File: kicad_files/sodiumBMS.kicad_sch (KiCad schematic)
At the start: 14 parts, among them J1 USB_C_Receptacle_PowerOnly_6P, U1 STM32F446RETx

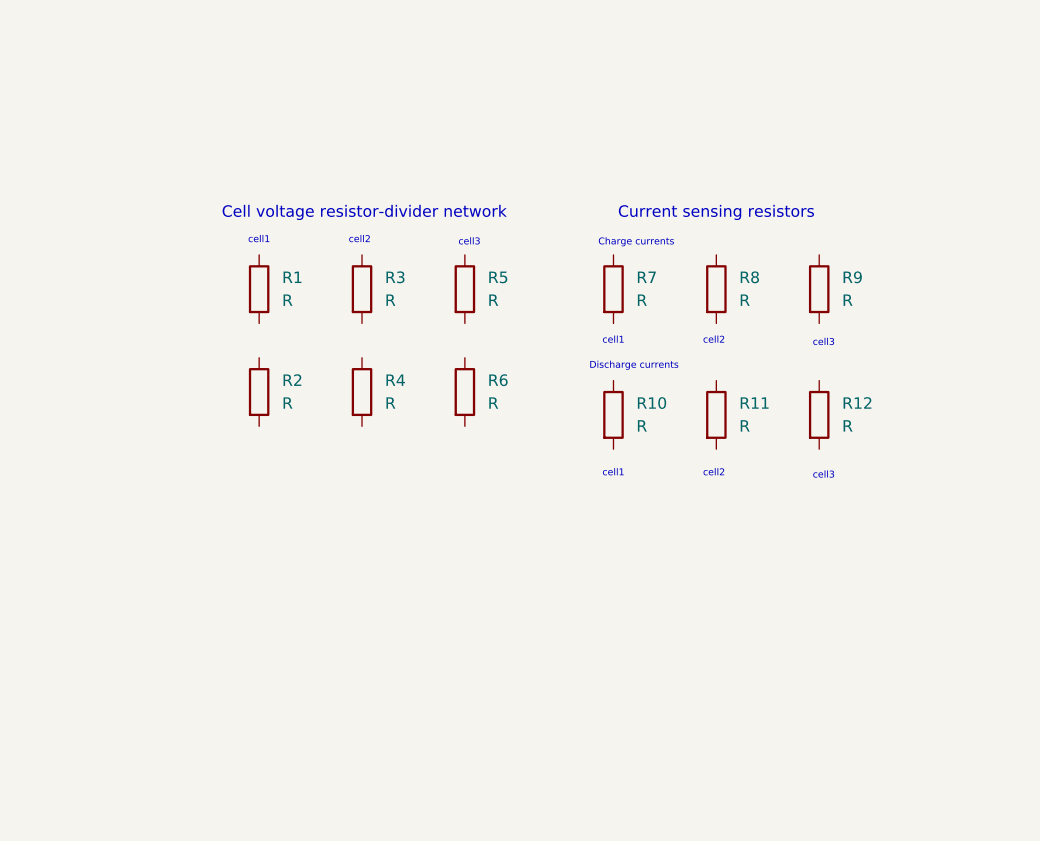
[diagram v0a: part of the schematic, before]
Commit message: added outputs for current and voltage sensing
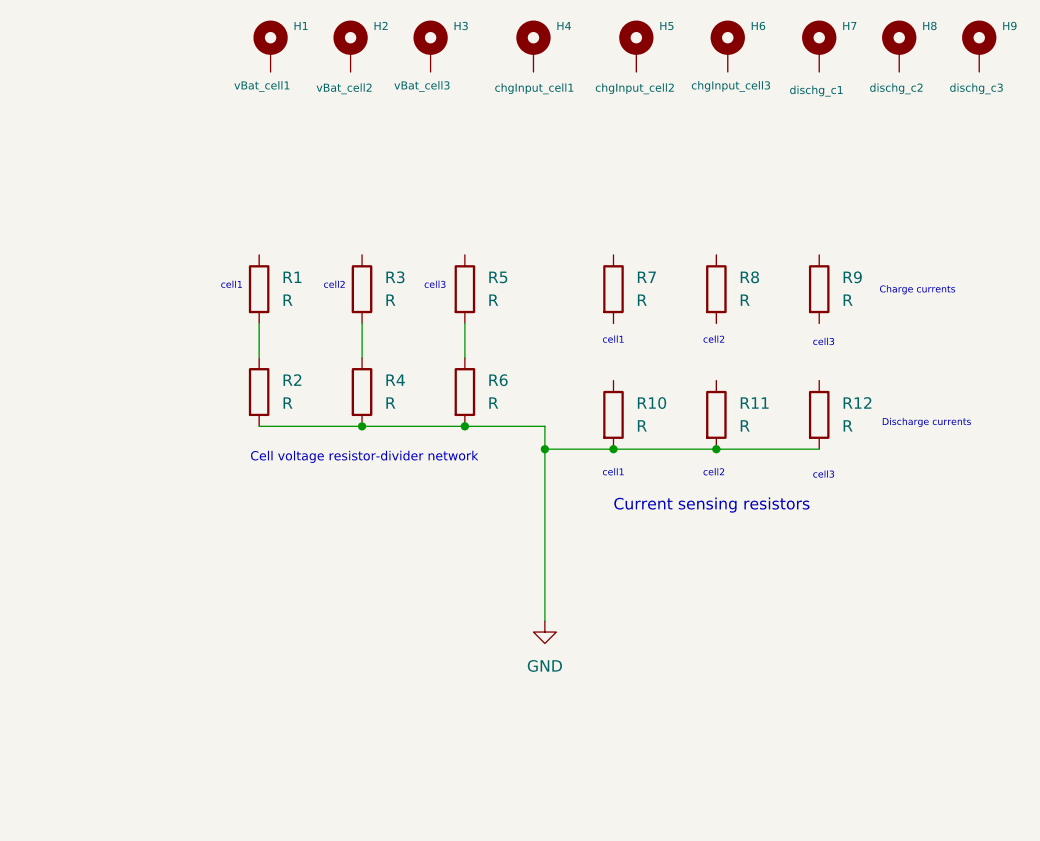
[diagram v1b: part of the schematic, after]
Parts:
- added H1: vBat_cell1, symbol Mechanical:MountingHole_Pad
- added H2: vBat_cell2, symbol Mechanical:MountingHole_Pad
- added H3: vBat_cell3, symbol Mechanical:MountingHole_Pad
- added H4: chgInput_cell1, symbol Mechanical:MountingHole_Pad
- added H5: chgInput_cell2, symbol Mechanical:MountingHole_Pad
- added H6: chgInput_cell3, symbol Mechanical:MountingHole_Pad
- added H7: dischg_c1, symbol Mechanical:MountingHole_Pad
- added H8: dischg_c2, symbol Mechanical:MountingHole_Pad
- added H9: dischg_c3, symbol Mechanical:MountingHole_Pad
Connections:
- net at R6.1: now also R5.2
- net GND: now reaches R6.2
- net GND: now also R10.2, R11.2, R12.2, R2.2, R4.2
- net at R2.1: now also R1.2
- net at R3.2: now also R4.1

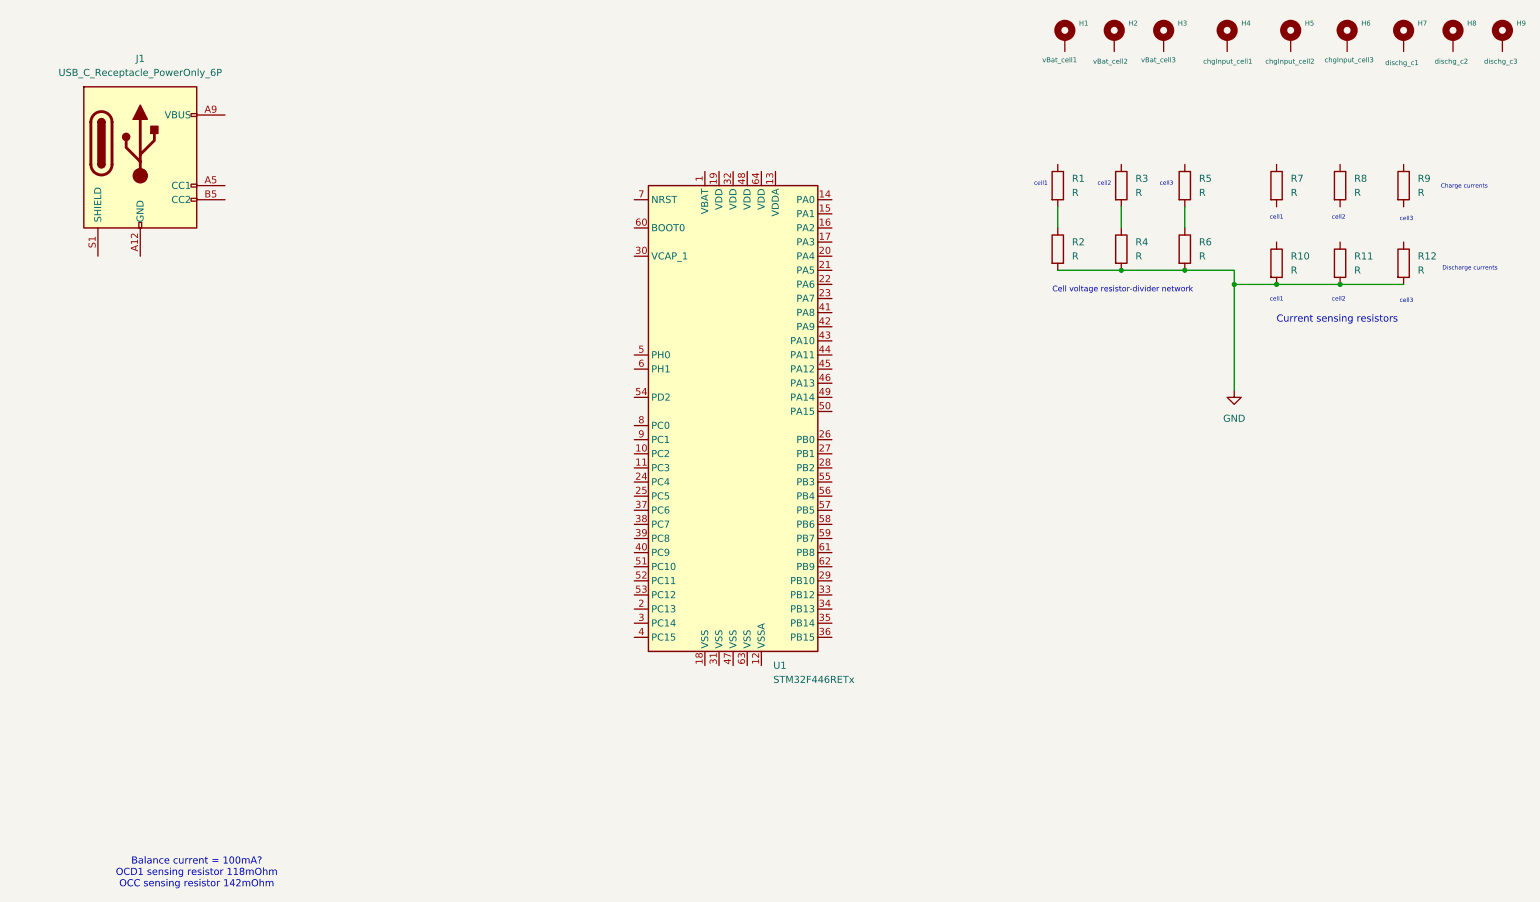
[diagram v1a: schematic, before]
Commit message: moved around the outputs on the schematic
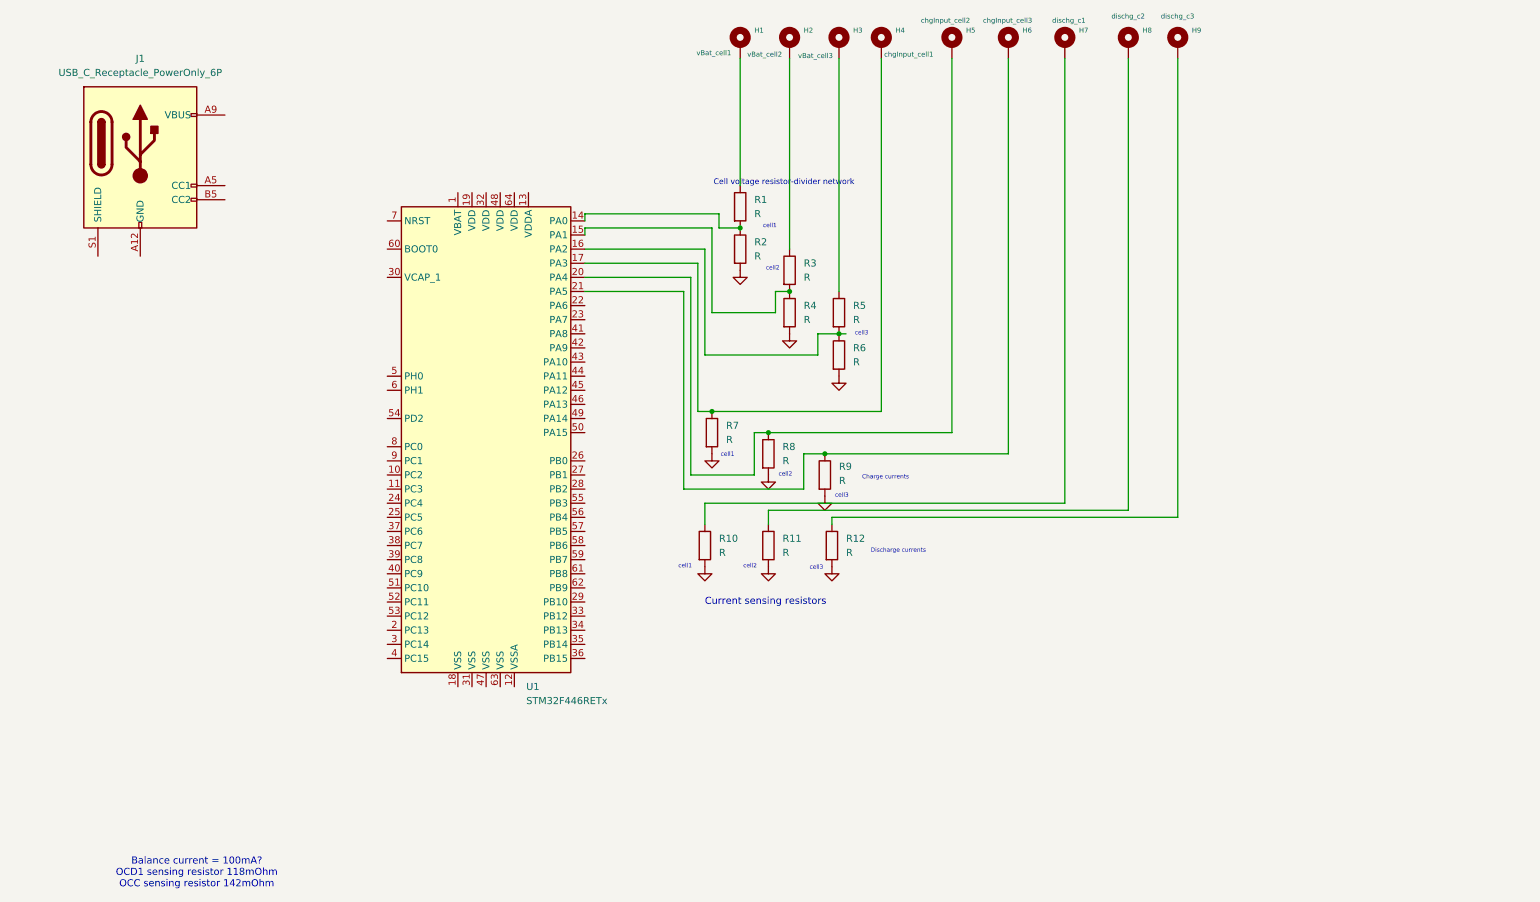
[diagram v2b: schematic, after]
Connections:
- net GND: now also R7.2, R8.2, R9.2
- net at R8.1: now also H5.1, U1.20 (PA4)
- net at R5.2, R6.1: now also U1.16 (PA2)
- net at H7.1: now also R10.1
- net at H1.1: now also R1.1
- net at H8.1: now also R11.1
- net at R9.1: now also H6.1, U1.21 (PA5)
- net at U1.14 (PA0): now also R1.2, R2.1
- net at U1.15 (PA1): now also R3.2, R4.1
- net at U1.17 (PA3): now also H4.1, R7.1
- net at H2.1: now also R3.1
- net at R5.1: now also H3.1
- net at R12.1: now also H9.1
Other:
- moved on the sheet: H1, H2, H3, H4, H5, H6, H7, H8, H9, R1, R10, R11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

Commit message: rearranged sch and added info about ICs
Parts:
- removed H6: chgInput_cell3, symbol Mechanical:MountingHole_Pad
- removed H7: dischg_c1, symbol Mechanical:MountingHole_Pad
- removed H8: dischg_c2, symbol Mechanical:MountingHole_Pad
- removed H9: dischg_c3, symbol Mechanical:MountingHole_Pad
- removed R10, R11, R12, R9: R, symbol Device:R
- added U2, U3: INA180A4, Package_TO_SOT_SMD:SOT-23-5, symbol Amplifier_Current:INA180A4
- H4: value chgInput_cell1 -> i_chg_sense
- H5: value chgInput_cell2 -> i_dchg_sense
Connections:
- net GND: now also U2.4 (-), U3.4 (-)
- net at H5.1, R8.1: now also U3.3 (+); no longer U1.20 (PA4)
- net at H4.1, R7.1: now also U2.3 (+); no longer U1.17 (PA3)
- net i_chg_sense: now reaches U1.22 (PA6)
- net i_chg_sense: now also U2.1
- new net 3.3V: U2.5 (V+)
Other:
- note removed: "Discharge currents"
- moved on the sheet: H5, R7, R8

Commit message: fixed readme formatting
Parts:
- R1, R3, R5: value R -> 20k
- R2, R4, R6: value R -> 100k
- R7, R8: value R -> 0.05
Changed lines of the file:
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@@
 			)
 		)
-		(property "Value" "R"
+		(property "Value" "0.05"
 			(at 215.9 24.1299 0)
 			(show_name no)
@@
 			)
 		)
-		(property "Value" "R"
+		(property "Value" "100k"
 			(at 162.56 74.9299 0)
 			(show_name no)
@@
 			)
 		)
-		(property "Value" "R"
+		(property "Value" "20k"
 			(at 162.56 67.3099 0)
 			(show_name no)
@@
 			)
 		)
-		(property "Value" "R"
+		(property "Value" "100k"
 			(at 144.78 55.8799 0)
 			(show_name no)
@@
 			)
 		)
-		(property "Value" "R"
+		(property "Value" "20k"
 			(at 153.67 59.6899 0)
 			(show_name no)
@@
 			)
 		)
-		(property "Value" "R"
+		(property "Value" "0.05"
 			(at 170.18 24.1299 0)
 			(show_name no)
@@
 			)
 		)
-		(property "Value" "R"
+		(property "Value" "100k"
 			(at 153.67 67.3099 0)
 			(show_name no)
@@
 			)
 		)
-		(property "Value" "R"
+		(property "Value" "20k"
 			(at 144.78 48.2599 0)
 			(show_name no)

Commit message: cleaning up some stuff
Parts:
- added C1, C2, C3: 1.5nF ish, symbol Device:C
- R7, R8: symbol Device:R -> Device:R_Shunt
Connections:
- net 3.3V: now also U3.5 (V+)
- net GND: now also R7.4, R8.4, U2.2 (GND), U3.2 (GND); no longer R7.2, R8.2, U2.4 (-), U3.4 (-)
- net at H5.1, R8.1: no longer U3.3 (+)
- net at H1.1, R1.1: now also C1.1, C1.2
- net i_dchg_sense: now reaches U1.23 (PA7)
- net i_dchg_sense: now also U3.1
- net at H2.1, R3.1: now also C2.1, C2.2
- net at H4.1, R7.1: no longer U2.3 (+)
- net at H3.1, R5.1: now also C3.1, C3.2
- new net: R8.2, U3.3 (+)
- new net: R8.3, U3.4 (-)
- new net: R7.2, U2.3 (+)
- new net: R7.3, U2.4 (-)
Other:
- note added: "Current sense amps - (actual part INA2180A4 - 2 channel version)"
- note added: "we want filter caps here because voltage is not super time sensitive"
- note removed: "Current sensing resistors"
- moved on the sheet: H5, J1, R1

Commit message: added LDO to schematic
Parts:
- added C4: 33uF, symbol Device:C
- added R10, R9: 5.1k, symbol Device:R
- added U4: LM3940, Package_TO_SOT_SMD:SOT-89-3, symbol Regulator_Linear:MCP1700x-330xxMB
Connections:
- net GND: now also J1.A12 (GND), J1.B12 (GND), J1.S1 (SHIELD), C4.2, R10.2, R9.2
- net at J1.A5 (CC1): now also R10.1
- net usb_5v_in: now reaches J1.A9 (VBUS), J1.B9 (VBUS)
- net usb_5v_in: now also U4.2 (VI)
- net at J1.B5 (CC2): now also R9.1
- net at U1.13 (VDDA): now also C4.1, U4.3 (VO)
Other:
- note added: "LDO goes here?"
- moved on the sheet: J1

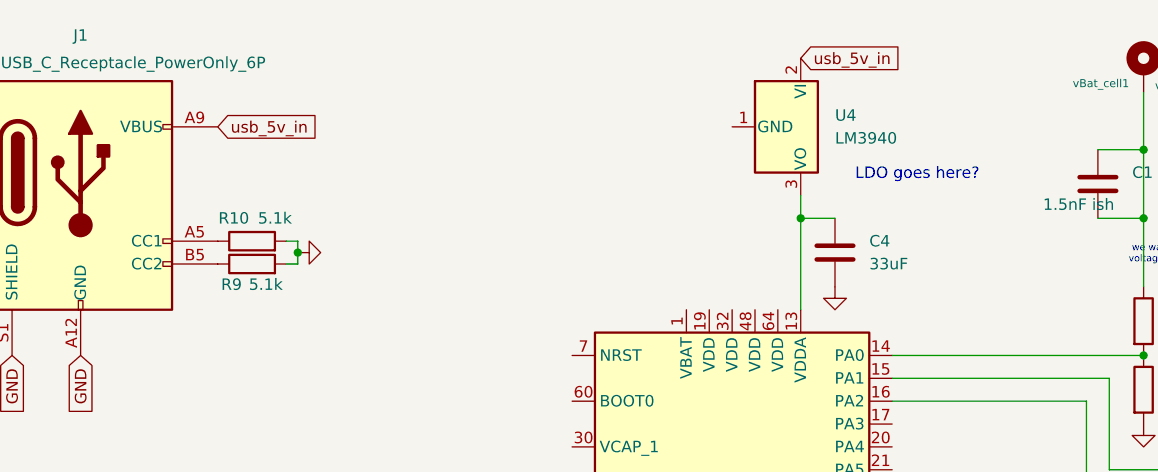
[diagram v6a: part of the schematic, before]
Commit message: more labelling and connections on sch
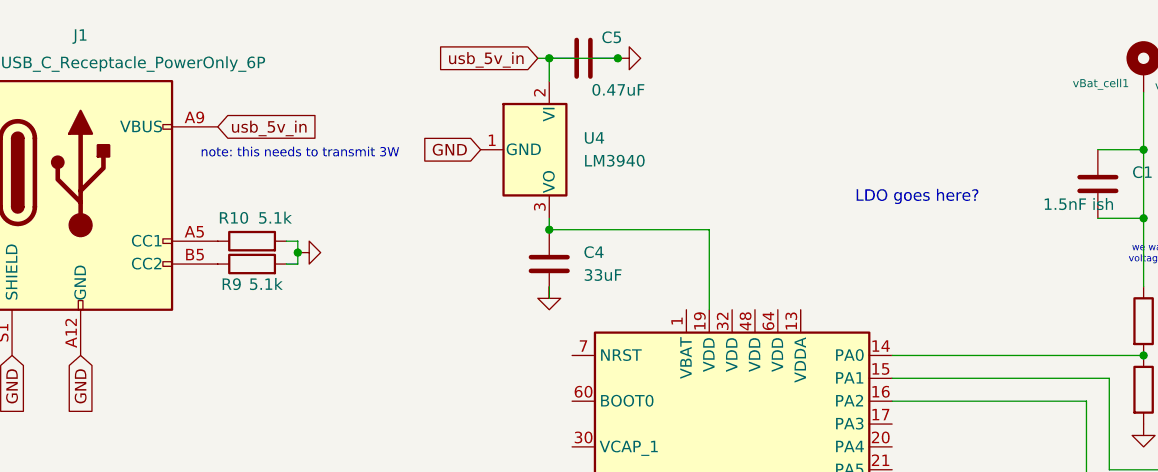
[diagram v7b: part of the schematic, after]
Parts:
- added C5: 0.47uF, symbol Device:C
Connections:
- net usb_5v_in is gone; now on net GND: J1.A9 (VBUS), J1.B9 (VBUS), U4.2 (VI)
- net GND: now also U4.1 (GND), C5.1, C5.2
- net at C4.1, U4.3 (VO): now also U1.19 (VDD); no longer U1.13 (VDDA)
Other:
- note added: "note: this needs to transmit 3W"
- moved on the sheet: C4, U4
